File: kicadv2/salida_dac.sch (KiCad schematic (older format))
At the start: 24 parts, among them J1 USB_B_Micro, J2 test_DAC, J7 test_I, J8 test_V, U7 TL064, U9 TL082

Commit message: planos de masa, gerber
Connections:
- net GND: no longer J1.5 (GND), J1.9 (Shield3), LPC1.1, LPC1.54
- new net GNDD: J1.5 (GND), J1.9 (Shield3), LPC1.1, LPC1.54
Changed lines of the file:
@@
-$EndComp
-$Comp
-L potenciostato-rescue:GND-power #PWR?
-U 1 1 6318DCCE
-P 750 1700
-AR Path="/60147E53/6318DCCE" Ref="#PWR?"  Part="1"
-AR Path="/6013BA2D/6318DCCE" Ref="#PWR011"  Part="1"
-F 0 "#PWR011" H 750 1450 50  0001 C CNN
-F 1 "GND" H 755 1523 50  0000 C CNN
-F 2 "" H 750 1700 50  0001 C CNN
-F 3 "" H 750 1700 50  0001 C CNN
-	1    750  1700
-	-1   0    0    -1
 $EndComp
 $Comp
@@
 	-1   0    0    -1
 $EndComp
-$Comp
-L potenciostato-rescue:GND-power #PWR?
-U 1 1 6318DCC8
-P 1600 3950
-AR Path="/60147E53/6318DCC8" Ref="#PWR?"  Part="1"
-AR Path="/6013BA2D/6318DCC8" Ref="#PWR014"  Part="1"
-F 0 "#PWR014" H 1600 3700 50  0001 C CNN
-F 1 "GND" H 1605 3773 50  0000 C CNN
-F 2 "" H 1600 3950 50  0001 C CNN
-F 3 "" H 1600 3950 50  0001 C CNN
-	1    1600 3950
-	-1   0    0    -1
-$EndComp
 Wire Wire Line
 	1800 3950 1600 3950
@@
 Wire Wire Line
 	5250 950  5250 1000
-$Comp
-L potenciostato-rescue:GND-power #PWR?
-U 1 1 6322CB06
-P 5250 1000
-AR Path="/6322CB06" Ref="#PWR?"  Part="1"
-AR Path="/6013BA2D/6322CB06" Ref="#PWR016"  Part="1"
-F 0 "#PWR016" H 5250 750 50  0001 C CNN
-F 1 "GND" H 5255 827 50  0000 C CNN
-F 2 "" H 5250 1000 50  0001 C CNN
-F 3 "" H 5250 1000 50  0001 C CNN
-	1    5250 1000
-	1    0    0    -1
-$EndComp
 Wire Wire Line
 	1900 6850 1700 6850
@@
 Wire Wire Line
 	1100 1700 1300 1700
+$Comp
+L power:GNDD #PWR0115
+U 1 1 636CF2B0
+P 1600 3950
+F 0 "#PWR0115" H 1600 3700 50  0001 C CNN
+F 1 "GNDD" H 1604 3795 50  0000 C CNN
+F 2 "" H 1600 3950 50  0001 C CNN
+F 3 "" H 1600 3950 50  0001 C CNN
+	1    1600 3950
+	1    0    0    -1
+$EndComp
+$Comp
+L power:GNDD #PWR0116
+U 1 1 636CF7F1
+P 750 1700
+F 0 "#PWR0116" H 750 1450 50  0001 C CNN
+F 1 "GNDD" H 754 1545 50  0000 C CNN
+F 2 "" H 750 1700 50  0001 C CNN
+F 3 "" H 750 1700 50  0001 C CNN
+	1    750  1700
+	1    0    0    -1
+$EndComp
+$Comp
+L power:GNDD #PWR0118
+U 1 1 636CFCCA
+P 5250 1000
+F 0 "#PWR0118" H 5250 750 50  0001 C CNN
+F 1 "GNDD" H 5254 845 50  0000 C CNN
+F 2 "" H 5250 1000 50  0001 C CNN
+F 3 "" H 5250 1000 50  0001 C CNN
+	1    5250 1000
+	1    0    0    -1
+$EndComp
 $EndSCHEMATC

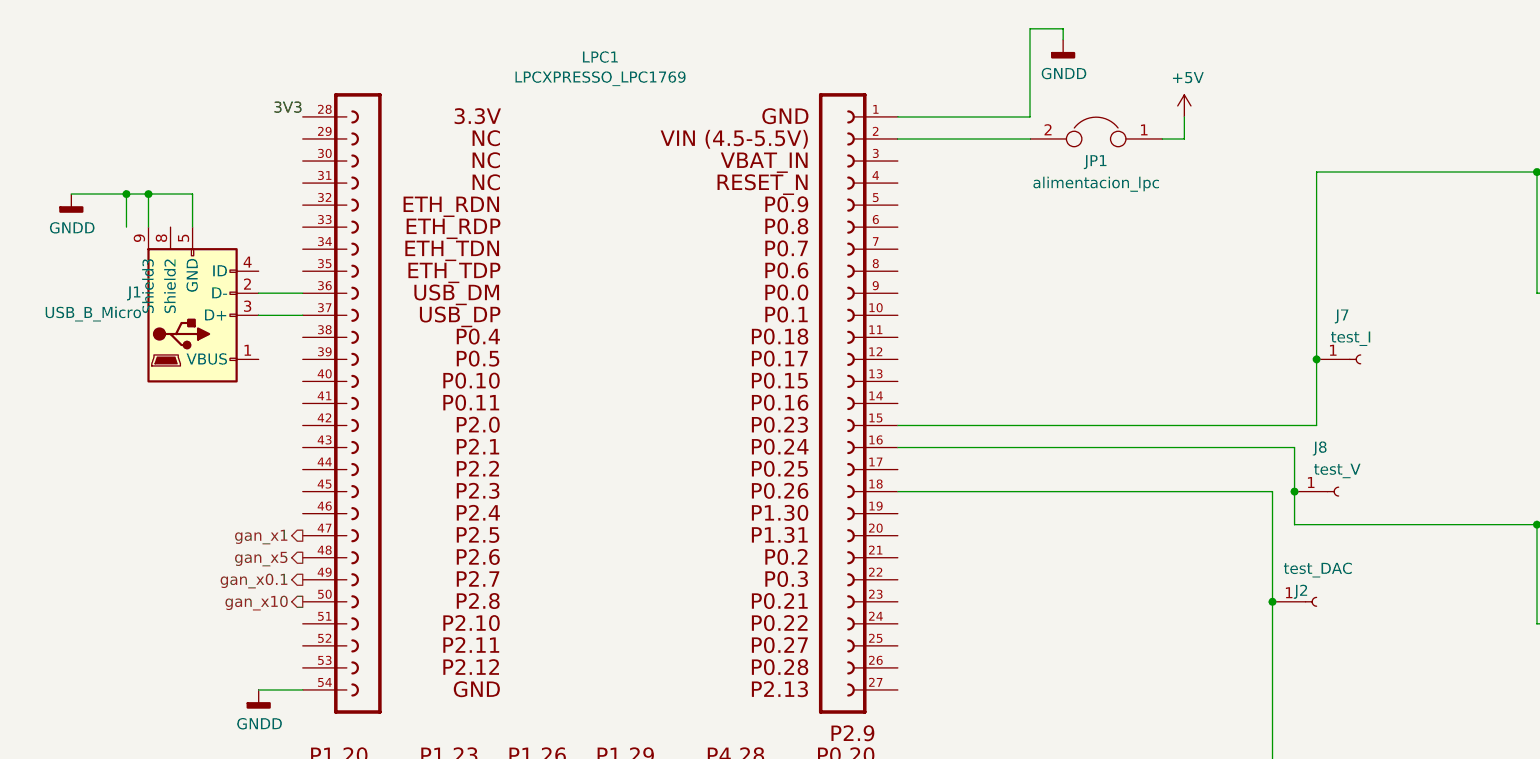
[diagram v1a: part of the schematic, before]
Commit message: finalizado (casi) f silk, falta mover BNC para que no choqeu con LPC
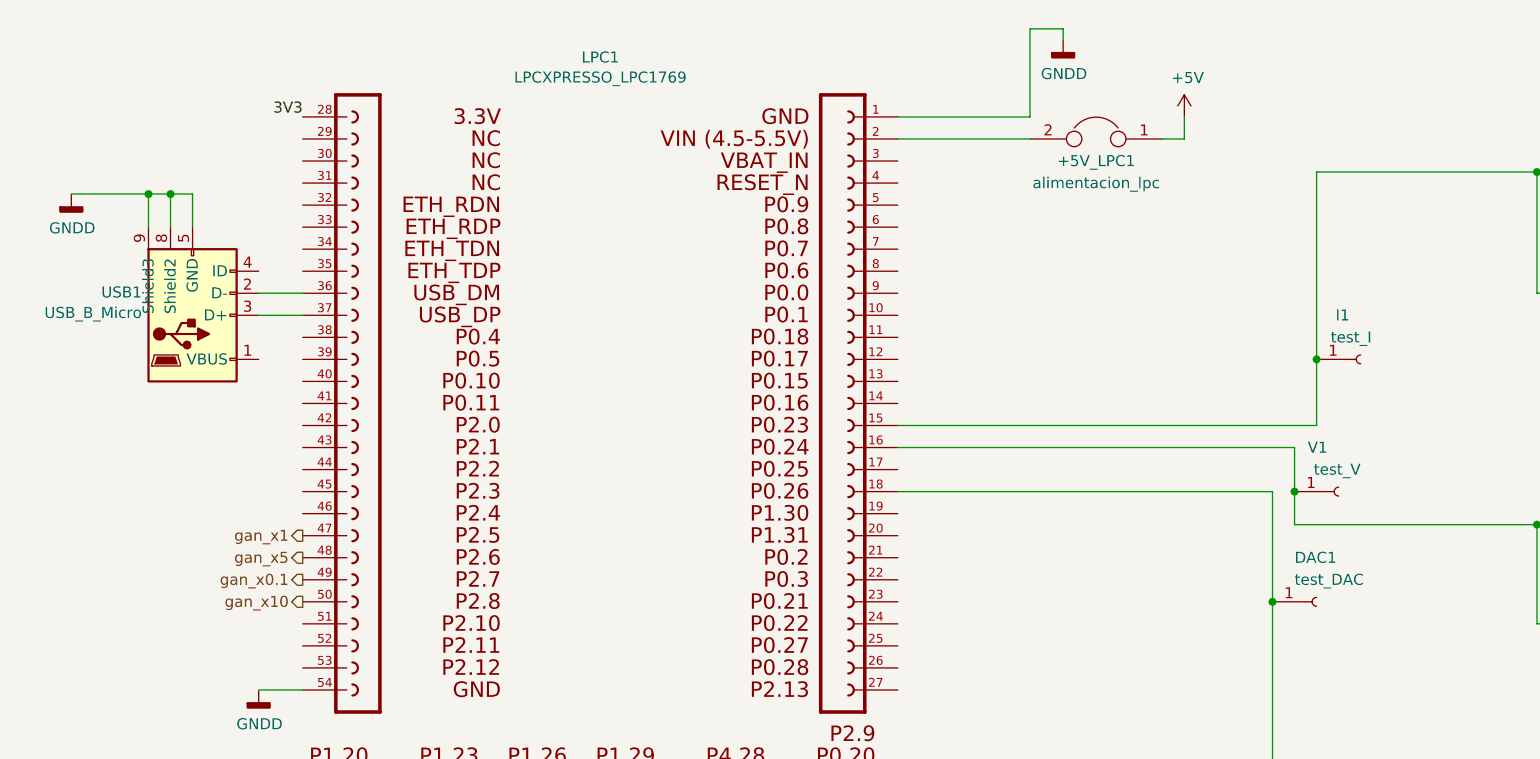
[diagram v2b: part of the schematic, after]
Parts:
- renumbered JP1 to +5V_LPC1, J2 to DAC1, J7 to I1, J1 to USB1, J8 to V1
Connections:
- net GNDD: now also USB1.8 (Shield2)
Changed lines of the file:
@@
 P 6400 3550
 AR Path="/60147E53/6318DCEB" Ref="J?"  Part="1"
-AR Path="/6013BA2D/6318DCEB" Ref="J2"  Part="1"
-F 0 "J2" H 6300 3500 50  0000 L CNN
-F 1 "test_DAC" H 6250 3400 50  0000 L CNN
+AR Path="/6013BA2D/6318DCEB" Ref="DAC1"  Part="1"
+F 0 "DAC1" H 6300 3350 50  0000 L CNN
+F 1 "test_DAC" H 6300 3450 50  0000 L CNN
 F 2 "Connector_PinHeader_2.54mm:PinHeader_1x01_P2.54mm_Vertical" H 6400 3550 50  0001 C CNN
 F 3 "~" H 6400 3550 50  0001 C CNN
@@
 AR Path="/6318DCB8" Ref="J?"  Part="1"
 AR Path="/60147E53/6318DCB8" Ref="J?"  Part="1"
-AR Path="/6013BA2D/6318DCB8" Ref="J1"  Part="1"
-F 0 "J1" H 1070 2146 50  0000 R CNN
+AR Path="/6013BA2D/6318DCB8" Ref="USB1"  Part="1"
+F 0 "USB1" H 1070 2146 50  0000 R CNN
 F 1 "USB_B_Micro" H 1070 2239 50  0000 R CNN
 F 2 "kicadv2:ModuloUSB-Micro" H 1450 2200 50  0001 C CNN
@@
 P 5400 1450
 AR Path="/60147E53/6318DCDD" Ref="JP?"  Part="1"
-AR Path="/6013BA2D/6318DCDD" Ref="JP1"  Part="1"
-F 0 "JP1" H 5400 1350 50  0000 C CNN
+AR Path="/6013BA2D/6318DCDD" Ref="+5V_LPC1"  Part="1"
+F 0 "+5V_LPC1" H 5400 1350 50  0000 C CNN
 F 1 "alimentacion_lpc" H 5400 1250 50  0000 C CNN
 F 2 "Connector_PinHeader_2.54mm:PinHeader_1x02_P2.54mm_Vertical" H 5400 1450 50  0001 C CNN
@@
 P 6500 3050
 AR Path="/60147E53/6318DCF3" Ref="J?"  Part="1"
-AR Path="/6013BA2D/6318DCF3" Ref="J8"  Part="1"
-F 0 "J8" H 6450 2850 50  0000 R CNN
+AR Path="/6013BA2D/6318DCF3" Ref="V1"  Part="1"
+F 0 "V1" H 6450 2850 50  0000 R CNN
 F 1 "test_V" H 6600 2950 50  0000 R CNN
 F 2 "Connector_PinHeader_2.54mm:PinHeader_1x01_P2.54mm_Vertical" H 6500 3050 50  0001 C CNN
@@
 P 6600 2450
 AR Path="/60147E53/6318DCE3" Ref="J?"  Part="1"
-AR Path="/6013BA2D/6318DCE3" Ref="J7"  Part="1"
-F 0 "J7" H 6550 2250 50  0000 R CNN
+AR Path="/6013BA2D/6318DCE3" Ref="I1"  Part="1"
+F 0 "I1" H 6550 2250 50  0000 R CNN
 F 1 "test_I" H 6650 2350 50  0000 R CNN
 F 2 "Connector_PinHeader_2.54mm:PinHeader_1x01_P2.54mm_Vertical" H 6600 2450 50  0001 C CNN
@@
 	3650 6850 3650 7250
 Wire Wire Line
-	750  1700 1000 1700
+	1200 1850 1200 1700
+Connection ~ 1100 1700
 Wire Wire Line
 	1100 1850 1100 1700
-Connection ~ 1100 1700
-Wire Wire Line
-	1000 1850 1000 1700
-Connection ~ 1000 1700
-Wire Wire Line
-	1000 1700 1100 1700
-Wire Wire Line
-	1100 1700 1300 1700
+Wire Wire Line
+	1100 1700 1200 1700
 $Comp
 L power:GNDD #PWR0115
@@
 	1    0    0    -1
 $EndComp
+Connection ~ 1200 1700
+Wire Wire Line
+	1200 1700 1300 1700
+Wire Wire Line
+	750  1700 1100 1700
 $EndSCHEMATC
